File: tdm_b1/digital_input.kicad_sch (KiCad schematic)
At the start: 8 parts, among them J10 Conn_Coaxial, U2 74LVC1G17

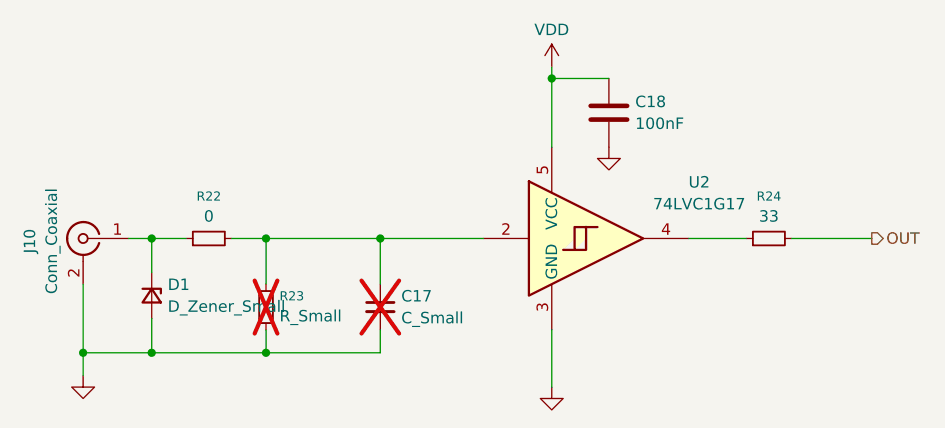
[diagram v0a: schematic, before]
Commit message: filled out part number for tdm_b1
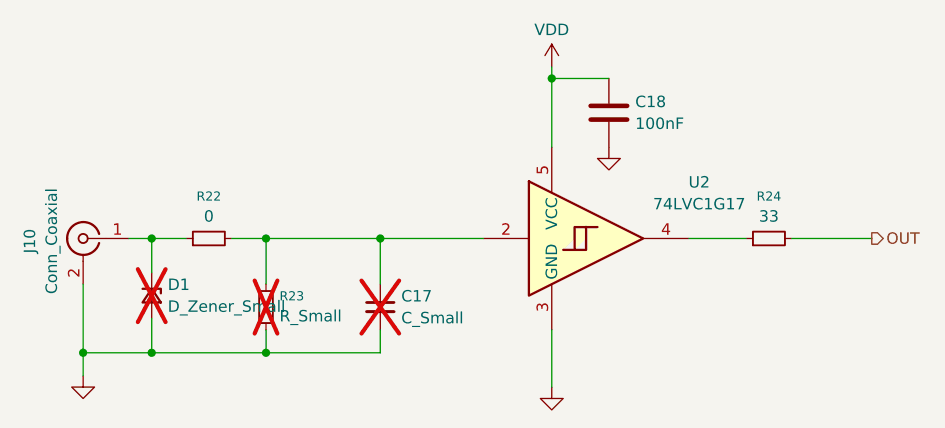
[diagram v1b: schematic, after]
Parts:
- C18: PN (none) -> GCJ188R71H104KA12D
- D1: now not fitted
- R22: PN (none) -> CRCW06030000Z0EA
- R24: PN (none) -> CRCW060333R0FKEAC
- U2: PN (none) -> SN74LVC1G17DBVR
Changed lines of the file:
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@@
+			)
+		)
+		(property "PN" "GCJ188R71H104KA12D"
+			(at 163.83 85.09 0)
+			(effects
+				(font
+					(size 1.27 1.27)
+				)
+				(hide yes)
 			)
 		)
@@
 			)
 		)
+		(property "PN" "CRCW06030000Z0EA"
+			(at 119.38 99.06 90)
+			(effects
+				(font
+					(size 1.27 1.27)
+				)
+				(hide yes)
+			)
+		)
 		(pin "2"
 		)
@@
 		)
 		(property "Description" "Single Schmitt Buffer Gate, Low-Voltage CMOS"
+			(at 162.56 99.06 0)
+			(effects
+				(font
+					(size 1.27 1.27)
+				)
+				(hide yes)
+			)
+		)
+		(property "PN" "SN74LVC1G17DBVR"
 			(at 162.56 99.06 0)
 			(effects
@@
 			)
 		)
+		(property "PN" "CRCW060333R0FKEAC"
+			(at 181.61 99.06 90)
+			(effects
+				(font
+					(size 1.27 1.27)
+				)
+				(hide yes)
+			)
+		)
 		(pin "2"
 		)
@@
 		(in_bom yes)
 		(on_board yes)
-		(dnp no)
+		(dnp yes)
 		(fields_autoplaced yes)
 		(property "Reference" "D1"
